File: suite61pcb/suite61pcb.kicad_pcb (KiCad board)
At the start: 2 copper layers, 1 part, among them U1 nice_nano

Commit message: create left pcb schematic
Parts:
- added REF**: 2-way joystick switch, marbastlib-various:2-way joystick switch, F.Cu at (62.7, 59.5)
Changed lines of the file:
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@@
   (net 26 "unconnected-(U1-Pad2)")
   (net 27 "unconnected-(U1-Pad1)")
+  (footprint "marbastlib-various:2-way joystick switch" (layer "F.Cu")
+    (at 62.70625 59.53125)
+    (attr smd)
+    (fp_text reference "REF**" (at 0 0 unlocked) (layer "F.SilkS")
+      (effects (font (size 1 1) (thickness 0.15)))
+    )
+    (fp_text value "2-way joystick switch" (at -0.2 2.2 unlocked) (layer "F.Fab")
+      (effects (font (size 1 1) (thickness 0.15)))
+    )
+    (fp_text user "GND" (at 2.4 6.2 unlocked) (layer "F.SilkS")
+      (effects (font (size 1 1) (thickness 0.15)))
+    )
+    (fp_text user "VCC" (at -6.6 6.2 unlocked) (layer "F.SilkS")
+      (effects (font (size 1 1) (thickness 0.15)))
+    )
+    (fp_text user "SW" (at -0.8 6.2 unlocked) (layer "F.SilkS")
+      (effects (font (size 1 1) (thickness 0.15)))
+    )
+    (fp_text user "UP" (at -4.2 -4.6 unlocked) (layer "F.SilkS")
+      (effects (font (size 1 1) (thickness 0.15)))
+    )
+    (fp_text user "dX" (at 5.6 6.2 unlocked) (layer "F.SilkS")
+      (effects (font (size 1 1) (thickness 0.15)))
+    )
+    (fp_text user "dY" (at -3.4 6.2 unlocked) (layer "F.SilkS")
+      (effects (font (size 1 1) (thickness 0.15)))
+    )
+    (fp_line (start -6.4 -3.6) (end -6.4 -3.8) (layer "F.SilkS") (width 0.12))
+    (fp_line (start -5.8 -4.6) (end -5.2 -3.8) (layer "F.SilkS") (width 0.12))
+    (fp_line (start -5.8 -4.6) (end -6.4 -3.6) (layer "F.SilkS") (width 0.12))
+    (fp_line (start -5.8 -0.4) (end -5.8 -4.6) (layer "F.SilkS") (width 0.12))
+    (fp_rect (start -9.4 10) (end 9 -7) (layer "F.SilkS") (width 0.12) (fill none))
+    (pad "1" smd roundrect (at -6.4 8.4 90) (size 2.286 1.524) (layers "F.Cu" "F.Paste" "F.Mask") (roundrect_rratio 0.25))
+    (pad "2" smd roundrect (at -3.4 8.4 90) (size 2.286 1.524) (layers "F.Cu" "F.Paste" "F.Mask") (roundrect_rratio 0.25))
+    (pad "3" smd roundrect (at -0.6 8.4 90) (size 2.286 1.524) (layers "F.Cu" "F.Paste" "F.Mask") (roundrect_rratio 0.25))
+    (pad "4" smd roundrect (at 2.4 8.4 90) (size 2.286 1.524) (layers "F.Cu" "F.Paste" "F.Mask") (roundrect_rratio 0.25))
+    (pad "5" smd roundrect (at 5.6 8.4 90) (size 2.286 1.524) (layers "F.Cu" "F.Paste" "F.Mask") (roundrect_rratio 0.25))
+  )
   (footprint "nice-nano-kicad-master:nice_nano" (layer "F.Cu")
     (at 30.1625 35.71875 -90)

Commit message: create .pcb
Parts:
- added D1: 1N4148W, Diode_SMD:D_SOD-123, F.Cu at (198.4, 87.3)
- added D10: 1N4148W, Diode_SMD:D_SOD-123, F.Cu at (212.9, 77.2)
- added D11: 1N4148W, Diode_SMD:D_SOD-123, F.Cu at (153.8, 137.7)
- added D12: 1N4148W, Diode_SMD:D_SOD-123, F.Cu at (155.2, 127.7)
- added D13: 1N4148W, Diode_SMD:D_SOD-123, F.Cu at (248.3, 44.9)
- added D14: 1N4148W, Diode_SMD:D_SOD-123, F.Cu at (158.1, 131.0)
- added D15: 1N4148W, Diode_SMD:D_SOD-123, F.Cu at (152.3, 131.0)
- added D16: 1N4148W, Diode_SMD:D_SOD-123, F.Cu at (192.7, 97.4)
- added D17: 1N4148W, Diode_SMD:D_SOD-123, F.Cu at (218.6, 73.8)
- added D18: 1N4148W, Diode_SMD:D_SOD-123, F.Cu at (148.1, 136.1)
- added D19: 1N4148W, Diode_SMD:D_SOD-123, F.Cu at (192.7, 87.3)
- added D2: 1N4148W, Diode_SMD:D_SOD-123, F.Cu at (198.4, 94.0)
- added D20: 1N4148W, Diode_SMD:D_SOD-123, F.Cu at (212.9, 73.8)
- added D21: 1N4148W, Diode_SMD:D_SOD-123, F.Cu at (185.6, 107.5)
- added D22: 1N4148W, Diode_SMD:D_SOD-123, F.Cu at (192.7, 94.0)
- added D23: 1N4148W, Diode_SMD:D_SOD-123, F.Cu at (179.8, 110.8)
- added D24: 1N4148W, Diode_SMD:D_SOD-123, F.Cu at (153.8, 134.4)
- added D25: 1N4148W, Diode_SMD:D_SOD-123, F.Cu at (136.6, 136.6)
- added D26: 1N4148W, Diode_SMD:D_SOD-123, F.Cu at (149.5, 127.7)
- added D27: 1N4148W, Diode_SMD:D_SOD-123, F.Cu at (172.5, 115.2)
- added D28: 1N4148W, Diode_SMD:D_SOD-123, F.Cu at (192.7, 90.7)
- added D29: 1N4148W, Diode_SMD:D_SOD-123, F.Cu at (218.6, 70.5)
- added D3: 1N4148W, Diode_SMD:D_SOD-123, F.Cu at (161.0, 127.7)
- added D30: 1N4148W, Diode_SMD:D_SOD-123, F.Cu at (218.6, 67.1)
- added D31: 1N4148W, Diode_SMD:D_SOD-123, F.Cu at (224.4, 67.1)
- added D32: 1N4148W, Diode_SMD:D_SOD-123, F.Cu at (172.5, 118.5)
- added D33: 1N4148W, Diode_SMD:D_SOD-123, F.Cu at (212.9, 70.5)
- added D34: 1N4148W, Diode_SMD:D_SOD-123, F.Cu at (204.2, 87.3)
- added D4: 1N4148W, Diode_SMD:D_SOD-123, F.Cu at (212.9, 67.1)
- added D5: 1N4148W, Diode_SMD:D_SOD-123, F.Cu at (140.8, 132.7)
- added D6: 1N4148W, Diode_SMD:D_SOD-123, F.Cu at (198.4, 90.7)
- added D7: 1N4148W, Diode_SMD:D_SOD-123, F.Cu at (179.8, 107.5)
- added D8: 1N4148W, Diode_SMD:D_SOD-123, F.Cu at (142.3, 136.1)
- added D9: 1N4148W, Diode_SMD:D_SOD-123, F.Cu at (146.6, 132.7)
- added J1: FFC_Receiver, LIB_503480-0500:5034800500, F.Cu at (173.3, 110.0)
- added J2: Joystick_FFC, marbastlib-various:joystick_switch, F.Cu at (240.1, 32.7)
- added J3: Battery JST, Connector_JST:JST_EH_B2B-EH-A_1x02_P2.50mm_Vertical, F.Cu at (87.2, 132.7)
- added J4: OLED, Connector_PinHeader_2.00mm:PinHeader_1x04_P2.00mm_Vertical, F.Cu at (81.6, 132.1)
- added JP1: Jumper_NO_Small, suite61:jumper, F.Cu at (73.2, 138.6)
- added JP2: Jumper_NO_Small, suite61:jumper, F.Cu at (147.4, 138.5)
- added JP3: Jumper_NO_Small, suite61:jumper, F.Cu at (140.2, 138.5)
- added JP4: Jumper_NO_Small, suite61:jumper, F.Cu at (143.8, 138.5)
- added JP5: Jumper_NO_Small, suite61:jumper, F.Cu at (202.1, 89.7)
- added JP6: Jumper_NO_Small, suite61:jumper, F.Cu at (230.9, 62.5)
- added JP7: Jumper_NO_Small, suite61:jumper, F.Cu at (222.2, 69.6)
- added JP8: Jumper_NO_Small, suite61:jumper, F.Cu at (69.5, 138.6)
- added JS1: Joycon_Joystick, suite61:2-way joystick switch, F.Cu at (259.6, 32.7)
- added LED1: SK6812MINI-E, marbastlib-various:LED_6028R, F.Cu at (142.3, 128.5)
- added LED2: SK6812MINI-E, marbastlib-various:LED_6028R, F.Cu at (88.0, 138.4)
- added LED3: SK6812MINI-E, marbastlib-various:LED_6028R, F.Cu at (105.4, 137.5)
- added LED4: SK6812MINI-E, marbastlib-various:LED_6028R, F.Cu at (122.7, 137.5)
- added LED5: SK6812MINI-E, marbastlib-various:LED_6028R, F.Cu at (96.7, 138.4)
- added LED6: SK6812MINI-E, marbastlib-various:LED_6028R, F.Cu at (114.0, 137.5)
- added R1: 4k7, Resistor_THT:R_Axial_DIN0207_L6.3mm_D2.5mm_P7.62mm_Horizontal, F.Cu at (81.2, 128.0)
- added R2: 4k7, Resistor_THT:R_Axial_DIN0207_L6.3mm_D2.5mm_P7.62mm_Horizontal, F.Cu at (70.4, 135.8)
- added S1: MSK12C02, LIB_MSK12C02:MSK12C02, F.Cu at (74.2, 130.9)
- added SW1: MX_SW_HS, marbastlib-mx:SW_MX_HS_1u, F.Cu at (99.0, 95.7)
- added SW10: MX_SW_HS, marbastlib-mx:SW_MX_HS_1u, F.Cu at (119.2, 35.2)
- added SW11: MX_SW_HS, marbastlib-mx:SW_MX_HS_1u, F.Cu at (179.7, 35.2)
- added SW12: MX_SW_HS, marbastlib-mx:SW_MX_HS_1u, F.Cu at (139.4, 35.2)
- added SW13: MX_SW_HS, marbastlib-mx:SW_MX_HS_1u, F.Cu at (159.6, 35.2)
- added SW14: MX_SW_HS, marbastlib-mx:SW_MX_HS_1u, F.Cu at (220.1, 35.2)
- added SW15: MX_SW_HS, marbastlib-mx:SW_MX_HS_1u, F.Cu at (139.4, 55.4)
- added SW16: MX_SW_HS, marbastlib-mx:SW_MX_HS_1u, F.Cu at (99.0, 115.9)
- added SW17: MX_SW_HS, marbastlib-mx:SW_MX_HS_1u, F.Cu at (139.4, 75.6)
- added SW18: MX_SW_HS, marbastlib-mx:SW_MX_HS_1u, F.Cu at (119.2, 75.6)
- added SW19: MX_SW_HS, marbastlib-mx:SW_MX_HS_1u, F.Cu at (78.9, 55.4)
- added SW2: MX_SW_HS, marbastlib-mx:SW_MX_HS_1u, F.Cu at (139.4, 95.7)
- added SW20: MX_SW_HS, marbastlib-mx:SW_MX_HS_1u, F.Cu at (159.6, 115.9)
- added SW21: MX_SW_HS, marbastlib-mx:SW_MX_HS_1u, F.Cu at (139.4, 115.9)
- added SW22: MX_SW_HS, marbastlib-mx:SW_MX_HS_1u, F.Cu at (199.9, 35.2)
- added SW23: MX_SW_HS, marbastlib-mx:SW_MX_HS_1u, F.Cu at (179.7, 95.7)
- added SW24: MX_SW_HS, marbastlib-mx:SW_MX_HS_1u, F.Cu at (78.9, 75.6)
- added SW25: MX_SW_HS, marbastlib-mx:SW_MX_HS_1u, F.Cu at (99.0, 55.4)
- added SW26: MX_SW_HS, marbastlib-mx:SW_MX_HS_1u, F.Cu at (78.9, 35.2)
- added SW27: MX_SW_HS, marbastlib-mx:SW_MX_HS_1u, F.Cu at (119.2, 95.7)
- added SW28: MX_SW_HS, marbastlib-mx:SW_MX_HS_1u, F.Cu at (159.6, 55.4)
- added SW29: MX_SW_HS, marbastlib-mx:SW_MX_HS_1u, F.Cu at (119.2, 115.9)
- added SW3: MX_SW_HS, marbastlib-mx:SW_MX_HS_1u, F.Cu at (179.7, 75.6)
- added SW30: MX_SW_HS, marbastlib-mx:SW_MX_HS_1u, F.Cu at (220.1, 55.4)
- added SW31: MX_SW_HS, marbastlib-mx:SW_MX_HS_1u, F.Cu at (179.7, 55.4)
- added SW32: MX_SW_HS, marbastlib-mx:SW_MX_HS_1u, F.Cu at (78.9, 115.9)
- added SW33: MX_SW_HS, marbastlib-mx:SW_MX_HS_1u, F.Cu at (99.0, 35.2)
- added SW34: MX_SW_HS, marbastlib-mx:SW_MX_HS_1u, F.Cu at (119.2, 55.4)
- added SW35: RotaryEncoder_Switch, marbastlib-various:ROT_Alps_EC11E-Switch, F.Cu at (237.8, 52.3)
- added SW36: Reset_Button, Button_Switch_SMD:SW_Push_1P1T_NO_CK_KMR2, F.Cu at (130.4, 137.3)
- added SW4: MX_SW_HS, marbastlib-mx:SW_MX_HS_1u, F.Cu at (99.0, 75.6)
- added SW5: MX_SW_HS, marbastlib-mx:SW_MX_HS_1u, F.Cu at (78.9, 95.7)
- added SW6: MX_SW_HS, marbastlib-mx:SW_MX_HS_1u, F.Cu at (199.9, 75.6)
- added SW7: MX_SW_HS, marbastlib-mx:SW_MX_HS_1u, F.Cu at (159.6, 95.7)
- added SW8: MX_SW_HS, marbastlib-mx:SW_MX_HS_1u, F.Cu at (159.6, 75.6)
- added SW9: MX_SW_HS, marbastlib-mx:SW_MX_HS_1u, F.Cu at (199.9, 55.4)
- added TH1: HOLE, MountingHole:MountingHole_3.7mm, F.Cu at (133.5, 130.5)
- added TH2: HOLE, MountingHole:MountingHole_3.7mm, F.Cu at (106.6, 130.5)
- added TH3: HOLE, MountingHole:MountingHole_3.7mm, F.Cu at (115.6, 130.5)
- added TH4: HOLE, MountingHole:MountingHole_3.7mm, F.Cu at (97.7, 130.5)
- added TH5: HOLE, MountingHole:MountingHole_3.7mm, F.Cu at (124.5, 130.5)
- moved REF** 23.8 mm to (86.5, 59.5)
- moved U1 17.3 mm to (40.5, 49.6)
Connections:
- U1 pad 1: unconnected-(U1-Pad1) -> LED
- U1 pad 10: unconnected-(U1-Pad10) -> col3
- U1 pad 11: unconnected-(U1-Pad11) -> col4
- U1 pad 12: unconnected-(U1-Pad12) -> col5
- U1 pad 13: unconnected-(U1-Pad13) -> row5
- U1 pad 14: unconnected-(U1-Pad14) -> row4
- U1 pad 15: unconnected-(U1-Pad15) -> row3
- U1 pad 16: unconnected-(U1-Pad16) -> row2
- U1 pad 17: unconnected-(U1-Pad17) -> row1
- U1 pad 18: unconnected-(U1-Pad18) -> row0
- U1 pad 19: unconnected-(U1-Pad19) -> JSY
- U1 pad 20: unconnected-(U1-Pad20) -> JSX
- U1 pad 21: unconnected-(U1-Pad21) -> VCC
- U1 pad 22: unconnected-(U1-Pad22) -> RESET
- U1 pad 23: unconnected-(U1-Pad23) -> GND
- U1 pad 24: unconnected-(U1-Pad24) -> BATTERY
- U1 pad 3: unconnected-(U1-Pad3) -> GND
- U1 pad 31: unconnected-(U1-Pad31) -> Enc0
- U1 pad 32: unconnected-(U1-Pad32) -> Enc1
- U1 pad 4: unconnected-(U1-Pad4) -> GND
- U1 pad 5: unconnected-(U1-Pad5) -> SDA
- U1 pad 6: unconnected-(U1-Pad6) -> SCL
- U1 pad 7: unconnected-(U1-Pad7) -> col0
- U1 pad 8: unconnected-(U1-Pad8) -> col1
- U1 pad 9: unconnected-(U1-Pad9) -> col2
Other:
- board outline added: 3.6 x 3.3 mm

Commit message: update pcb
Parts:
- removed J2: Joystick_FFC, marbastlib-various:joystick_switch
- removed JS1: Joycon_Joystick, suite61:2-way joystick switch
- removed REF**: 2-way joystick switch, marbastlib-various:2-way joystick switch
- SW2, SW29: footprint marbastlib-mx:SW_MX_HS_1u -> marbastlib-mx:SW_MX_HS_1.5u
- SW23: footprint marbastlib-mx:SW_MX_HS_1u -> marbastlib-mx:SW_MX_1.5u; moved to B.Cu
- SW3: footprint marbastlib-mx:SW_MX_HS_1u -> marbastlib-mx:SW_MX_1.75u; moved to B.Cu
- SW36, U1: moved to B.Cu
- SW4, SW6: footprint marbastlib-mx:SW_MX_HS_1u -> suite61:SW_MX_P_2.25u; moved to B.Cu
- SW7: footprint marbastlib-mx:SW_MX_HS_1u -> marbastlib-mx:SW_MX_1u; moved to B.Cu
- moved U1 220.8 mm to (261.1, 42.4)
- moved S1 207.3 mm to (252.3, 24.6), turned to 180 degrees
- moved JP6 200.4 mm to (59.6, 166.6)
- moved R2 199.1 mm to (243.7, 37.8), turned to -90 degrees
- moved R1 189.9 mm to (247.7, 36.6), turned to -90 degrees
- moved SW36 178.3 mm to (268.3, 24.3), turned to 180 degrees
- moved JP5 174.1 mm to (48.3, 171.3)
- moved SW32 152.2 mm to (223.8, 69.6)
- moved SW33 135.8 mm to (223.8, 88.7)
- moved SW29 133.6 mm to (252.1, 102.2)
- moved SW24 133.4 mm to (204.8, 31.5)
- moved JP7 131.5 mm to (141.0, 173.0)
- moved SW26 130.5 mm to (204.8, 69.6)
- moved SW19 107.0 mm to (185.7, 50.6)
- moved SW25 105.8 mm to (204.8, 50.6)
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
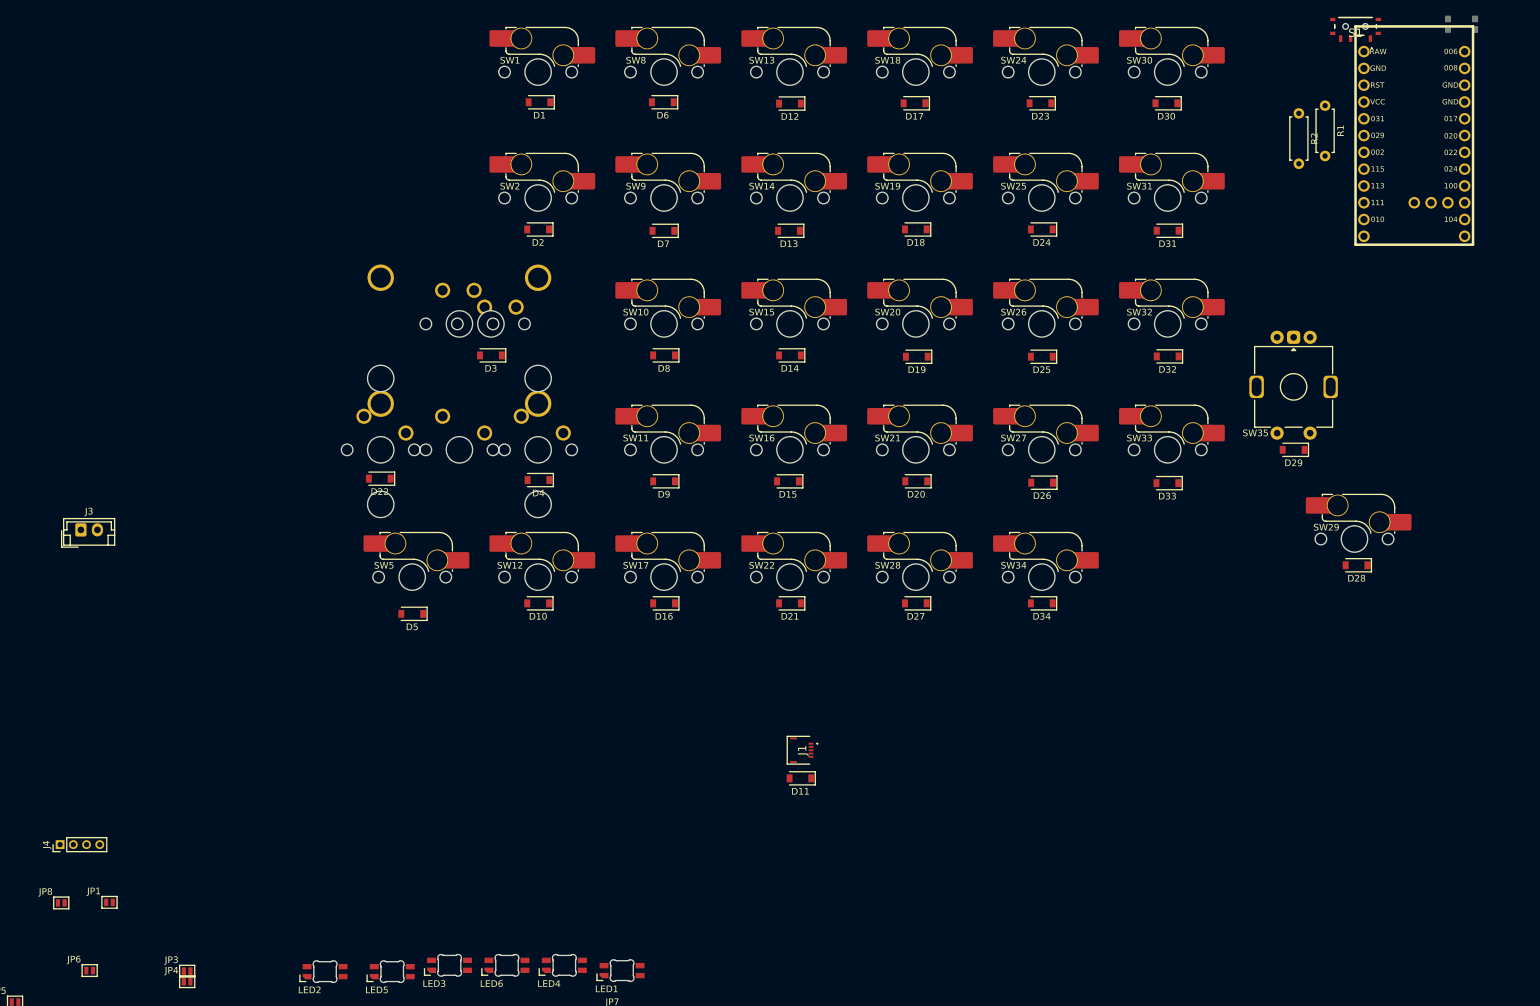
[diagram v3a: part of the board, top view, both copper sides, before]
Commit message: update pcb and add keebio submod
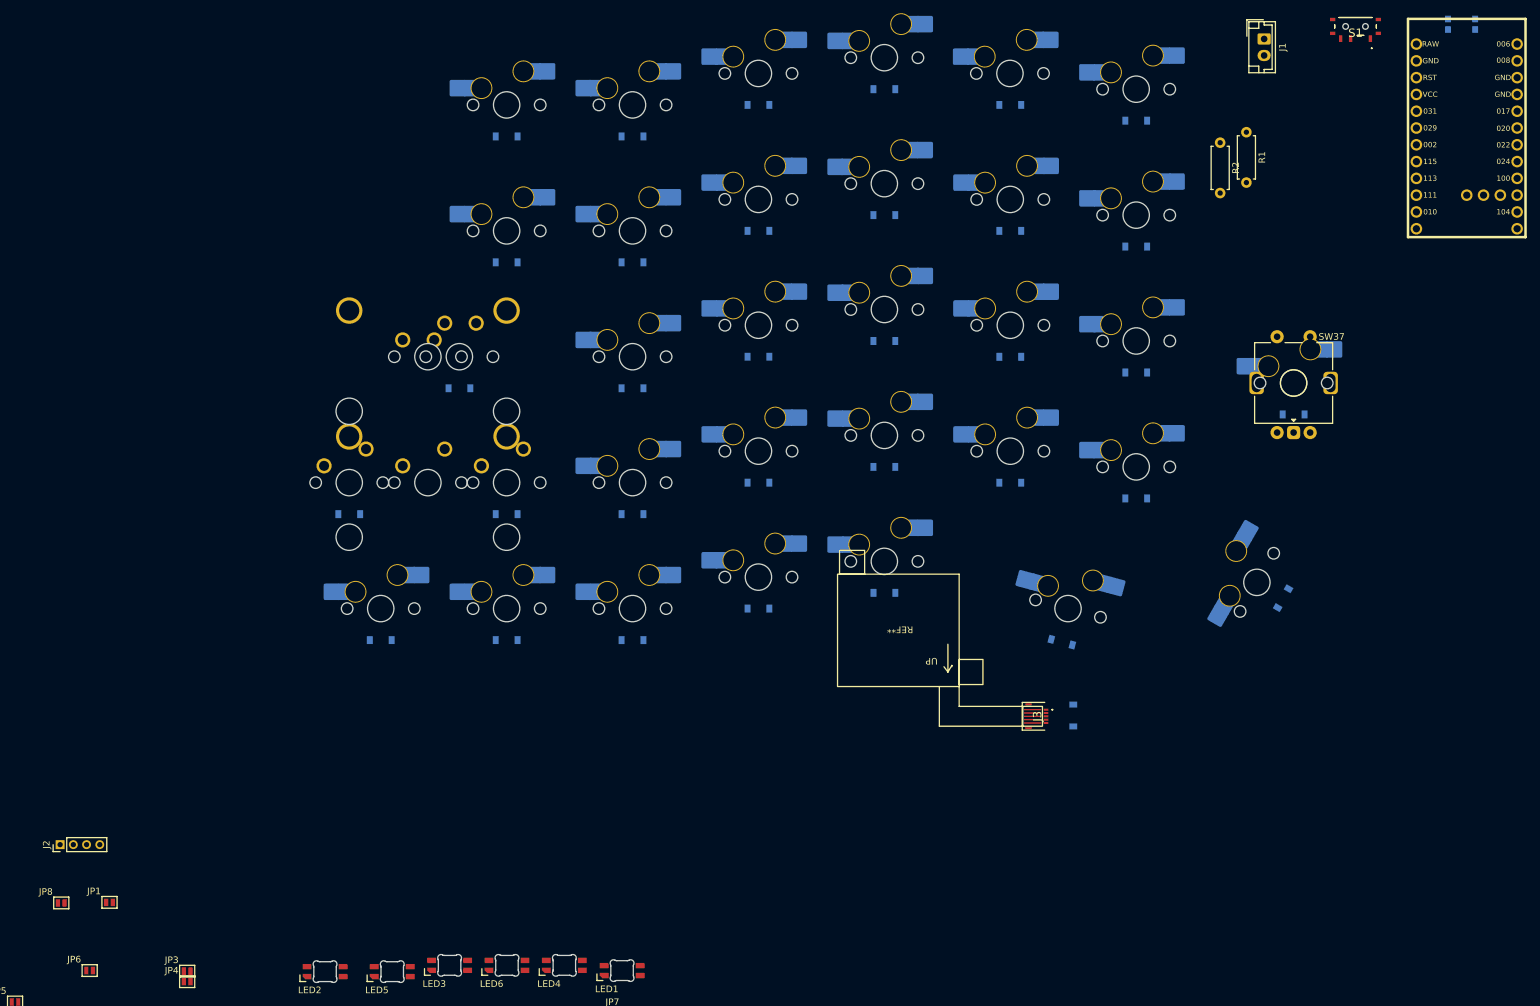
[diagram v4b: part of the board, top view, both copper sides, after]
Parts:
- added REF**: 2-way joystick switch, suite61:2-way joystick switch, F.Cu at (192.1, 113.5)
- added SW36: MX_SW_HS, marbastlib-mx:SW_MX_HS_1u, B.Cu at (242.9, 78.6)
- D1, SW1: moved to B.Cu
- D10: renamed from D18; moved to B.Cu
- D11: renamed from D24; moved to B.Cu
- D12: renamed from D31; moved to B.Cu
- D13: renamed from D3; moved to B.Cu
- D14: renamed from D8; moved to B.Cu
- D15: renamed from D14; moved to B.Cu
- D16: renamed from D19; moved to B.Cu
- D17: renamed from D25; moved to B.Cu
- D18: renamed from D32; moved to B.Cu
- D19: renamed from D4; moved to B.Cu
- D2: renamed from D6; moved to B.Cu
- D20: renamed from D9; moved to B.Cu
- D21: renamed from D15; moved to B.Cu
- D22: renamed from D20; moved to B.Cu
- D23: renamed from D26; moved to B.Cu
- D24: renamed from D33; moved to B.Cu
- D25: renamed from D5; moved to B.Cu
- D26: renamed from D10; moved to B.Cu
- D27: renamed from D16; moved to B.Cu
- D28: renamed from D21; moved to B.Cu
- D29: renamed from D27; moved to B.Cu
- D3: renamed from D12; moved to B.Cu
- D30: renamed from D34; moved to B.Cu
- D31: renamed from D22; moved to B.Cu
- D32: renamed from D28; moved to B.Cu
- D33: renamed from D11; moved to B.Cu
- D34: renamed from D29; moved to B.Cu
- D4: renamed from D17; moved to B.Cu
- D5: renamed from D23; moved to B.Cu
- D6: renamed from D30; moved to B.Cu
- D7: renamed from D2; moved to B.Cu
- D8: renamed from D7; moved to B.Cu
- D9: renamed from D13; moved to B.Cu
- SW10: renamed from SW19; moved to B.Cu
- SW11: renamed from SW25; moved to B.Cu
- SW12: renamed from SW31; moved to B.Cu
- SW13: renamed from SW3; value MX_SW_HS -> MX_SW; moved to F.Cu
- SW14: renamed from SW6; value MX_SW_HS -> MX_SW; moved to F.Cu
- SW15: renamed from SW10; moved to B.Cu
- SW16: renamed from SW15; moved to B.Cu
- SW17: renamed from SW20; moved to B.Cu
- SW18: renamed from SW26; moved to B.Cu
- SW19: renamed from SW32; moved to B.Cu
- SW2: renamed from SW8; moved to B.Cu
- SW21: renamed from SW4; value MX_SW_HS -> MX_SW; moved to F.Cu
- SW22: renamed from SW7; value MX_SW_HS -> MX_SW; moved to F.Cu
- SW23: renamed from SW11; moved to B.Cu
- SW24: renamed from SW16; moved to B.Cu
- SW25: renamed from SW21; moved to B.Cu
- SW26: renamed from SW27; moved to B.Cu
- SW27: renamed from SW33; moved to B.Cu
- SW28: renamed from SW5; moved to B.Cu
- SW29: renamed from SW12; moved to B.Cu
- SW3: renamed from SW13; moved to B.Cu
- SW30: renamed from SW17; moved to B.Cu
- SW31: renamed from SW22; moved to B.Cu
- SW32: renamed from SW28; moved to B.Cu
- SW33: renamed from SW34; moved to B.Cu
- SW34: renamed from SW23; moved to F.Cu
- SW35: renamed from SW29; moved to B.Cu
- SW4: renamed from SW18; moved to B.Cu
- SW5: renamed from SW24; moved to B.Cu
- SW6: renamed from SW30; moved to B.Cu
- SW7: renamed from SW2; moved to B.Cu
- SW8: renamed from SW9; moved to B.Cu
- SW9: renamed from SW14; moved to B.Cu
- moved J1 193.8 mm to (238.4, 26.5), turned to -90 degrees
- moved D33 42.4 mm to (209.6, 128.9), turned to -90 degrees
- moved J3 35.9 mm to (203.8, 129.0)
- moved SW35 16.2 mm to (237.3, 108.7), turned to -120 degrees
- moved R2 12.7 mm to (231.8, 42.2)
- moved R1 12.6 mm to (235.7, 40.6)
- moved D32 12.2 mm to (241.3, 111.1), turned to 60 degrees
- moved U1 8.02 mm to (269.1, 41.3)
- moved D27 7.33 mm to (142.9, 117.5), turned to 0 degrees
- moved D26 7.32 mm to (123.8, 117.5), turned to 0 degrees
- moved D1 7.16 mm to (123.8, 41.3), turned to 0 degrees
- moved D31 7.08 mm to (100.0, 98.4), turned to 0 degrees
- moved D19 7.05 mm to (123.8, 98.4), turned to 0 degrees
- moved D2 6.91 mm to (142.9, 41.3), turned to 0 degrees
- moved SW8 6.89 mm to (142.9, 55.6), turned to 180 degrees
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- renumbered J3 to J1, J4 to J2, J1 to J3, SW36 to SW20, SW35 to SW37

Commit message: update pcb and schematic
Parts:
- removed R1, R2: 4k7, Resistor_THT:R_Axial_DIN0207_L6.3mm_D2.5mm_P7.62mm_Horizontal
- added C1: 100nF, Capacitor_SMD:C_0805_2012Metric, F.Cu at (202.0, 65.8)
- added C2: 100nF, Capacitor_SMD:C_0805_2012Metric, F.Cu at (204.4, 65.8)
- added D31: 1N4148W, Diode_SMD:D_SOD-123, B.Cu at (188.8, 119.9)
- J1: footprint Connector_JST:JST_EH_B2B-EH-A_1x02_P2.50mm_Vertical -> Connector_JST:JST_EH_S2B-EH_1x02_P2.50mm_Horizontal
- JP5, JP6, JP7, JP8: moved to B.Cu
- LED1, LED2, LED3, LED4, LED5, LED6: footprint marbastlib-various:LED_6028R -> LED_SMD:LED_SK6812MINI_PLCC4_3.5x3.5mm_P1.75mm
- SW37: footprint marbastlib-various:ROT_Alps_EC11E-Switch -> Keebio-Parts:RotaryEncoder_EC11
- moved JP5 191.5 mm to (207.9, 65.5), turned to 90 degrees
- moved JP8 182.8 mm to (213.9, 65.5), turned to 90 degrees
- moved JP6 181.1 mm to (209.9, 65.5), turned to 90 degrees
- moved JP2 180.2 mm to (208.1, 65.5), turned to 90 degrees
- moved J2 177.1 mm to (213.0, 66.1), turned to -90 degrees
- moved JP4 171.9 mm to (212.1, 65.5), turned to 90 degrees
- moved JP1 169.8 mm to (206.1, 65.5), turned to 90 degrees
- moved JP3 169.3 mm to (210.1, 65.5), turned to 90 degrees
- moved LED2 132.3 mm to (140.4, 42.9)
- moved JP7 128.8 mm to (211.9, 65.5), turned to 90 degrees
- moved LED1 127.1 mm to (176.2, 45.2)
- moved LED3 117.6 mm to (100.8, 50.0)
- moved LED6 90.4 mm to (191.2, 106.4)
- moved LED5 72.5 mm to (138.1, 102.4)
- moved LED4 67.5 mm to (100.8, 107.2)
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- renumbered D31 to D32, D32 to D33, D33 to D34, D34 to D35
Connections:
- D32 pad 1: Net-(D33-Pad2) (its old number) -> row5
- D33 pad 1: Net-(D33-Pad2) (its old number) -> row5
- D34 pad 2: Net-(D33-Pad2) (its old number) -> Net-(D34-Pad2)
- D35 pad 1: Net-(D33-Pad2) (its old number) -> row5
- D35 pad 2: Net-(D34-Pad2) -> Net-(SW37-PadS2)
- J3 pad 1: col3 -> VCC
- J3 pad 3: Net-(D33-Pad2) (its old number) -> Net-(D34-Pad2)
- S1 pad B1: Net-(J1-Pad2) -> BATTERY
- S1 pad C1: BATTERY -> Net-(J1-Pad2)
- SW36 pad 1: col0 -> Net-(SW37-PadS2)
- SW36 pad 2: Net-(D34-Pad2) -> col0
- SW37 pad S1: Net-(D34-Pad2) -> col0
- SW37 pad S2: col0 -> Net-(SW37-PadS2)
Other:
- board size 3.6 x 3.3 mm -> 189.6 x 115.8 mm
